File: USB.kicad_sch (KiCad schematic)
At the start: 54 parts, among them J3 USB_C_Receptacle_USB2.0, J4 USB_A_Stacked, Q4 BC817, U10 TPD4EUSB30, U4 CP2102N-Axx-xQFN24, U5 FSUSB30MUX, U6 FSUSB30MUX, U7 FE1.1, U8 TPD4EUSB30, U9 AP2191W, Y1 12MHz{slash}10pF

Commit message: Weeded out all ERC errors
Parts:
- removed C10, C9: 4u7, Capacitor_SMD:C_0402_1005Metric, symbol Device:C_Small
- removed C11, C112, C113, C12, C4: 100n, Capacitor_SMD:C_0402_1005Metric, symbol Device:C_Small
- removed C111: 10u, Capacitor_SMD:C_0805_2012Metric, symbol Device:C_Small
- removed C6: 1u, Capacitor_SMD:C_0402_1005Metric, symbol Device:C_Small
- removed D30, D31: CDBQR0130L, Diode_SMD:D_0402_1005Metric, symbol Device:D_Schottky_Small
- removed J4: USB_A_Stacked, Connector_USB:USB_A_Wuerth_61400826021_Horizontal_Stacked, symbol Yellow:USB_A_Stacked
- removed JP1: Conn_01x03_Male, Connector_PinHeader_2.54mm:PinHeader_1x03_P2.54mm_Vertical, symbol Jumper:Jumper_3_Bridged12
- removed Q4: BC817, Package_TO_SOT_SMD:SOT-23, symbol Transistor_BJT:BC817
- removed R27: 10R, Resistor_SMD:R_0402_1005Metric, symbol Device:R_Small
- removed R28, R54: 0R, Resistor_SMD:R_0402_1005Metric, symbol Device:R_Small
- removed R3, R55: 1k, Resistor_SMD:R_0402_1005Metric, symbol Device:R_Small
- removed R4, R6, R7: 2k2/1%, Resistor_SMD:R_0402_1005Metric, symbol Device:R_Small
- removed R41: 100R, Resistor_SMD:R_0402_1005Metric, symbol Device:R_Small
- removed R5: 3k6, Resistor_SMD:R_0402_1005Metric, symbol Device:R_Small
- removed R61, R8: 10k, Resistor_SMD:R_0402_1005Metric, symbol Device:R_Small
- removed TP2, TP3: TestPoint, TestPoint:TestPoint_Pad_D1.0mm, symbol Connector:TestPoint
- removed U4: CP2102N-Axx-xQFN24, Package_DFN_QFN:QFN-24-1EP_4x4mm_P0.5mm_EP2.6x2.6mm, symbol Interface_USB:CP2102N-Axx-xQFN24
- removed U5: FSUSB30MUX, Package_SO:MSOP-10_3x3mm_P0.5mm, symbol Yellow:FSUSB30MUX
- removed U7: FE1.1, Package_QFP:TQFP-48_7x7mm_P0.5mm, symbol Yellow:FE1.1
- removed U9: AP2191W, Package_TO_SOT_SMD:SOT-23-5, symbol Power_Management:AP2171W
- added C314: 100nF, Capacitor_SMD:C_0402_1005Metric, symbol Device:C_Small
- added J302, J303: USB_A, Hatlabs:USB-A-TH_ZCJB-HJ, symbol Connector:USB_A
- added Q301: BC817, Package_TO_SOT_SMD:SOT-23, symbol Transistor_BJT:BC817
- added R301: 2.7k, Resistor_SMD:R_0603_1608Metric, symbol Device:R_Small
- added R302: 1k, Resistor_SMD:R_0402_1005Metric, symbol Device:R_Small
- added R306: 10k, Resistor_SMD:R_0402_1005Metric, symbol Device:R_Small
- added R308: 15k, Resistor_SMD:R_0402_1005Metric, symbol Device:R_Small
- added U302: FE1.1S-BQFN24B, Package_DFN_QFN:QFN-24-1EP_4x4mm_P0.5mm_EP2.5x2.5mm, symbol Hatlabs:FE1.1S-BQFN24B
- added U305: AP22653W6-7, Package_TO_SOT_SMD:SOT-23-6, symbol Hatlabs:AP22653
- C301: renamed from C2; value 100n -> 100nF; LCSC (none) -> C1525
- C302: renamed from C7; value 10p -> 10pF; LCSC (none) -> C32949
- C303: renamed from C8; value 10p -> 10pF; LCSC (none) -> C32949
- C304: renamed from C1; value 100n -> 100nF; LCSC (none) -> C1525
- C305: renamed from C5; value 10u -> 10uF; LCSC (none) -> C15850
- C306: renamed from C3; value 100n -> 100nF; LCSC (none) -> C1525
- C307: renamed from C17; value 47u -> 47uF; LCSC (none) -> C16780
- C308: renamed from C18; value 47u -> 47uF; LCSC (none) -> C16780
- C309: renamed from C14; value 10u -> 10uF; LCSC (none) -> C15850
- C310: renamed from C19; value 10u -> 10uF; LCSC (none) -> C15850
- C311: renamed from C15; value 100n -> 100nF; LCSC (none) -> C1525
- C312: renamed from C20; value 10u -> 10uF; LCSC (none) -> C15850
- C313: renamed from C21; value 100n -> 100nF; LCSC (none) -> C1525
- J301: renamed from J3; footprint Connector_USB:USB_C_Receptacle_HRO_TYPE-C-31-M-12 -> HALSER:Shou Han Type-C 16P LTH6.8; symbol Connector:USB_C_Receptacle_USB2.0 -> Connector:USB_C_Receptacle_USB2.0_16P; LCSC (none) -> C5187468; Manufacturer HRO -> (none); PartNumber TYPE-C-31-M-12 -> (none)
- R303: renamed from R11; value 2.7k/1% -> 2.7k; footprint Resistor_SMD:R_0402_1005Metric -> Resistor_SMD:R_0603_1608Metric; LCSC (none) -> C13167
- R304: renamed from R13; value 5k1 -> 5.1k; LCSC (none) -> C25905
- R305: renamed from R14; value 5k1 -> 5.1k; LCSC (none) -> C25905
- R310: renamed from R62; LCSC (none) -> C25744
- U301: renamed from U6; value FSUSB30MUX -> TP3USB30M10; LCSC (none) -> C2959840; Manufacturer ON Semiconductor -> TECH PUBLIC; PartNumber FSUSB30MUX -> TP3USB30M10
- U303: renamed from U8; LCSC (none) -> C558427
- U304: renamed from U10; LCSC (none) -> C558427
- Y301: renamed from Y1; value 12MHz/10pF -> 12MHz/10pF; LCSC (none) -> C50430
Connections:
- net OTG.D+ is gone; now on net USB-C.D+: U301.3 (HSD2+)
- net OTG.D- is gone; now on net USB-C.D-: U301.7 (HSD2-)
- net +3V3: now also C304.2, C305.2, U302.16 (~{XRSTJ}), U302.17 (VBUSM), U302.18 (BUSJ), U302.20 (VD33F); no longer C304.1, C305.1
- net +5V: now also C309.1, C311.1, U305.1 (IN); no longer C309.2, C311.2
- net GND: now also C304.1, C305.1, C309.2, C311.2, C314.2, J302.4 (GND), J302.5 (Shield), J303.4 (GND), J303.5 (Shield), Q301.2 (E), R301.1, R308.2, U302.25 (VSS), U305.2 (GND); no longer C304.2, C305.2, C309.1, C311.1
- net HUB.D+: now also U302.15 (DPU)
- net HUB.D-: now also U302.14 (DMU)
- net USB0.D+: now also J302.3 (D+), U302.10 (DP2)
- net USB0.D-: now also J302.2 (D-), U302.9 (DM2)
- net USB1.D+: now also J303.3 (D+), U302.12 (DP1)
- net USB1.D-: now also J303.2 (D-), U302.11 (DM1)
- net VBUS: now also R301.2
- net VBUS_{OUT}: now also C314.1, J302.1 (VBUS), J303.1 (VBUS), U305.6 (OUT)
- net ~{USB_OC}: now also U302.1 (~{OVCJ}), U305. (~{FAULT})
- net at C302.1, Y301.3: now also U302.3 (XOUT)
- net at C303.1, Y301.1: now also U302.4 (XIN)
- net at R303.2: now also U302.13 (REXT)
- net CM4_USB_D+ renamed D+
- net CM4_USB_D- renamed D-
- net CM4_USB_OTG_ID renamed OTG_ID
- new net: Q301.1 (B), R302.1
- new net: R308.1, U305.5 (ILIM)
- new net CMx_3V3: R306.1
- new net EN: Q301.3 (C), R306.2, U305.3 (EN)
- new net ~{USB_PWR_EN}: R302.2, U302.24 (~{PWRJ})
- no-connect marks 26 -> 12
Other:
- note added: "AP22653 EN is active-high."
- note added: "USB-C Receptacle and ESD protection USB 2.0 Peripheral operation only"
- note removed: "CP2102N USB <-> UART For CM4 serial console"
- note removed: "For break signalling"
- note removed: "NOTE: Place 10uF cap. close to the pin 26 and 0.1uF close to pin 3, 13."
- note removed: "USB-C Receptacle and ESD protection USB 2.0 Peripheral operataion only"
- note removed: "USB-C peripheral mode selection switch 1-2 USB-C <-> CP2102N 3-2 USB-C <-> CM4 OTG"
- company: Nabu Casa -> Hat Labs Oy
- title: USB 2.0 host/USB 2.0 device -> HALPI2
- moved on the sheet: C301, C302, C303, C304, C305, C306, C307, C308, C309, C310, C311, C312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

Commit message: Implement ideal diodes for input and LDO power ORing
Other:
- note added: "MUX selecting between USB peripheral and host mode (using different ports as well)"
- note added: "USB 2.0 HUB for host mode use"
- moved on the sheet: C301, C302, C303, C304, C305, C306, C309, C311, J301, R301, R303, R304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

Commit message: Re-annotate schematics
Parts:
- renumbered C306 to C305, C305 to C306, C309 to C307, C307 to C309, C311 to C310, C312 to C311, C310 to C312, C314 to C313, C313 to C314, R303 to R302, R304 to R303, R305 to R304, R302 to R305, R308 to R307, R310 to R308

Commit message: Sprinkle test points on the schematics
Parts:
- added TP301, TP302, TP303: TestPoint, TestPoint:TestPoint_Pad_D1.0mm, symbol Connector:TestPoint
- J301: footprint HALSER:Shou Han Type-C 16P LTH6.8 -> Hatlabs:USB_TYPE-C_SHOU-HAN_16PLT-H6.8
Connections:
- net VBUS_{OUT}: now also TP303.1
- net ~{USB_OC}: now also TP302.1
- net ~{USB_PWR_EN}: now also TP301.1

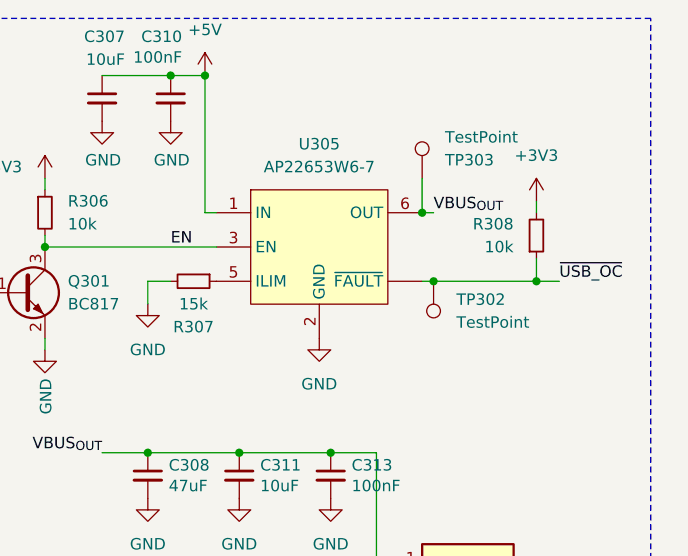
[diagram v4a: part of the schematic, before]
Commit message: Fix ethernet port & other changes
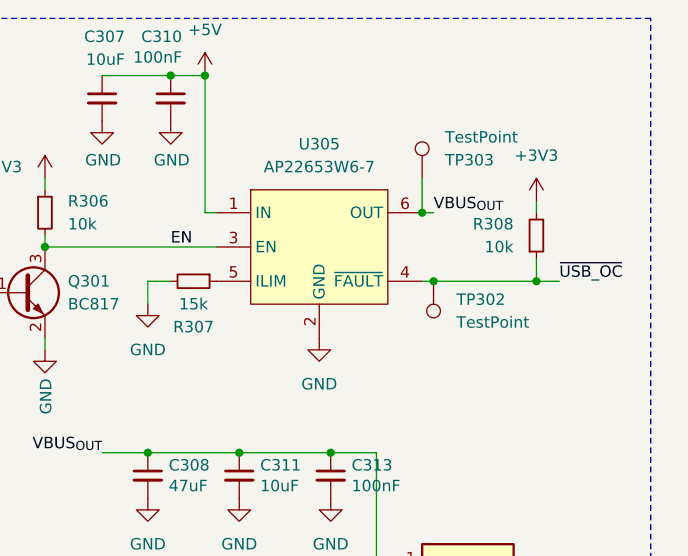
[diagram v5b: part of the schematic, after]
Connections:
- net ~{USB_OC}: now also U305.4 (~{FAULT}); no longer U305. (~{FAULT})
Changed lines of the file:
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@@
 			)
 		)
-		(pin ""
+		(pin "4"
 		)
 		(pin "5"

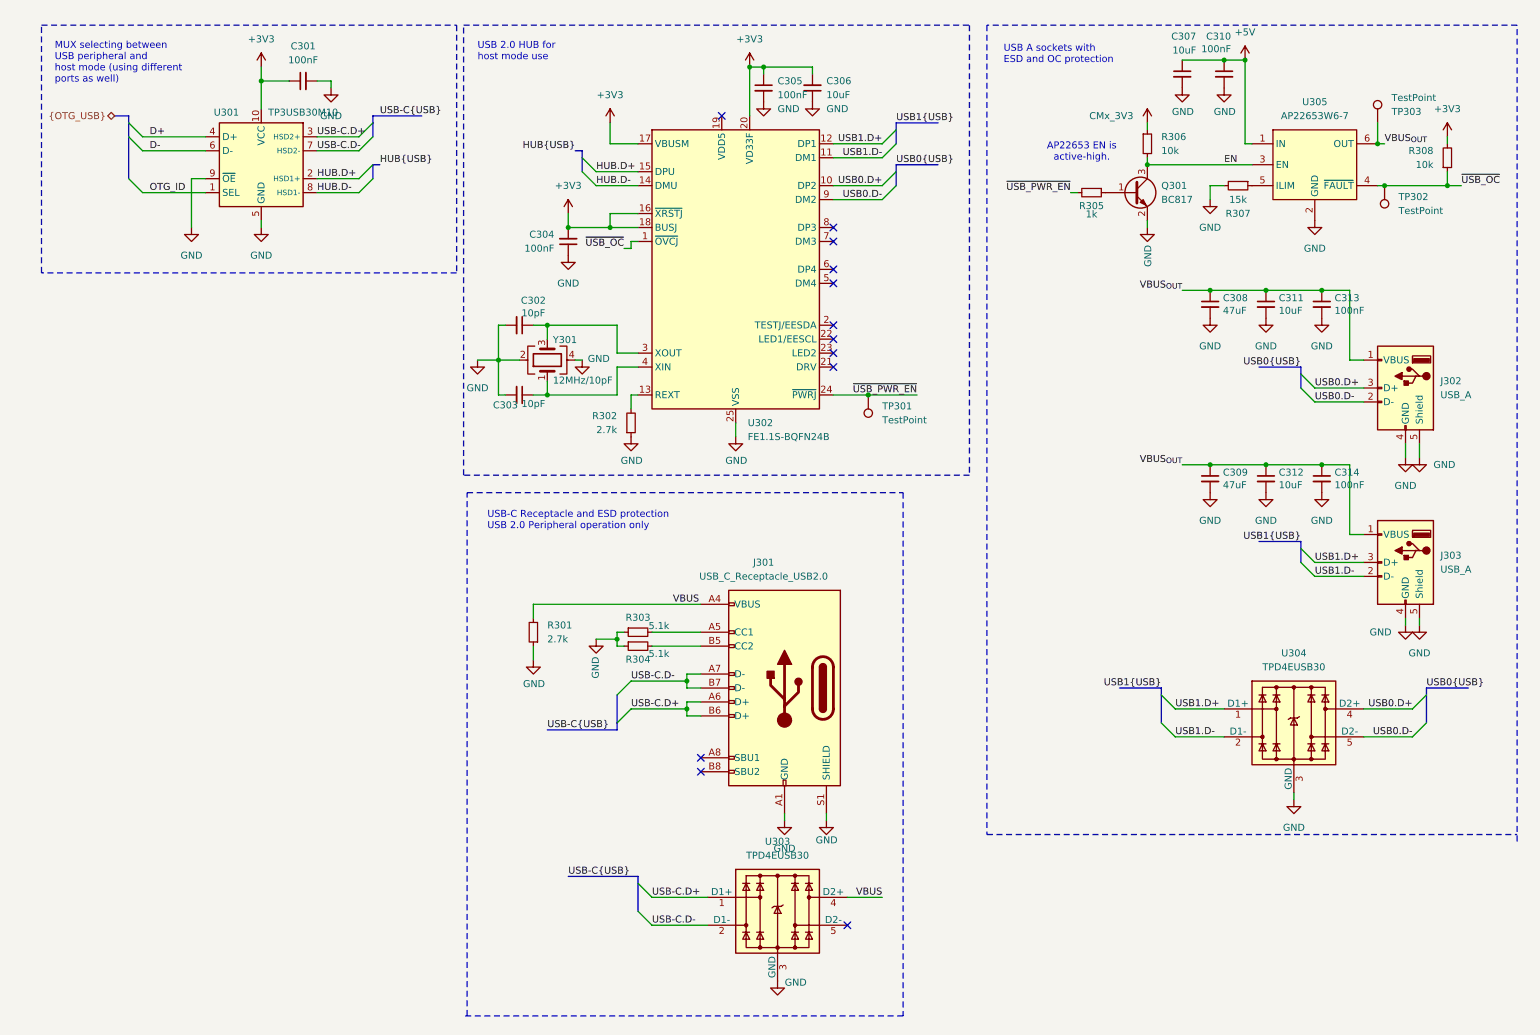
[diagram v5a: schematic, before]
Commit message: Reserve USB 2 for peripheral use only
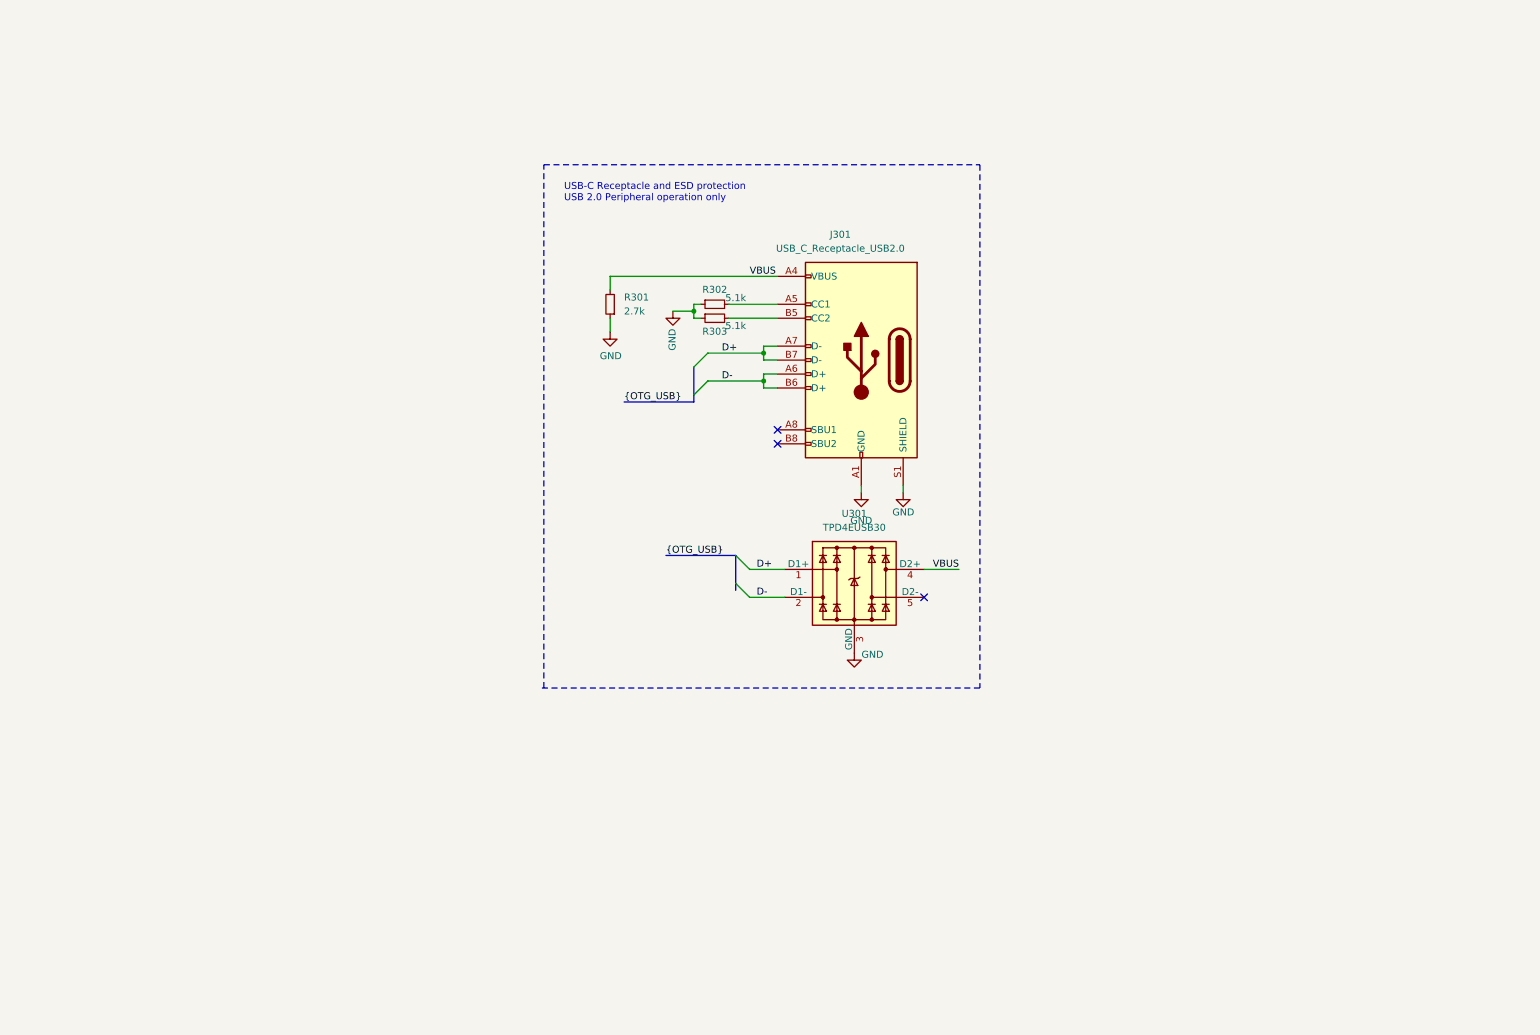
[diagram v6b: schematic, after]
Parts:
- removed C301, C304, C305, C310, C313, C314: 100nF, Capacitor_SMD:C_0402_1005Metric, symbol Device:C_Small
- removed C302, C303: 10pF, Capacitor_SMD:C_0402_1005Metric, symbol Device:C_Small
- removed C306, C307, C311, C312: 10uF, Capacitor_SMD:C_0805_2012Metric, symbol Device:C_Small
- removed C308, C309: 47uF, Capacitor_SMD:C_0805_2012Metric, symbol Device:C_Small
- removed J302, J303: USB_A, Hatlabs:USB-A-TH_ZCJB-HJ, symbol Connector:USB_A
- removed Q301: BC817, Package_TO_SOT_SMD:SOT-23, symbol Transistor_BJT:BC817
- removed R304: 5.1k, Resistor_SMD:R_0402_1005Metric, symbol Device:R_Small
- removed R305: 1k, Resistor_SMD:R_0402_1005Metric, symbol Device:R_Small
- removed R306, R308: 10k, Resistor_SMD:R_0402_1005Metric, symbol Device:R_Small
- removed R307: 15k, Resistor_SMD:R_0402_1005Metric, symbol Device:R_Small
- removed TP301, TP302, TP303: TestPoint, TestPoint:TestPoint_Pad_D1.0mm, symbol Connector:TestPoint
- removed U301: TP3USB30M10, Package_SO:MSOP-10_3x3mm_P0.5mm, symbol Yellow:FSUSB30MUX
- removed U302: FE1.1S-BQFN24B, Package_DFN_QFN:QFN-24-1EP_4x4mm_P0.5mm_EP2.5x2.5mm, symbol Hatlabs:FE1.1S-BQFN24B
- removed U303, U304: TPD4EUSB30, Package_SON:USON-10_2.5x1.0mm_P0.5mm, symbol Yellow:TPD4EUSB30
- removed U305: AP22653W6-7, Package_TO_SOT_SMD:SOT-23-6, symbol Hatlabs:AP22653
- removed Y301: 12MHz/10pF, Crystal:Crystal_SMD_3225-4Pin_3.2x2.5mm, symbol Device:Crystal_GND24
- added U301: TPD4EUSB30, Package_SON:USON-10_2.5x1.0mm_P0.5mm, symbol Yellow:TPD4EUSB30
- R302: value 2.7k -> 5.1k; footprint Resistor_SMD:R_0603_1608Metric -> Resistor_SMD:R_0402_1005Metric; LCSC C13167 -> C25905
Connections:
- net USB-C.D+ is gone; now on net D-: J301.A6 (D+), J301.B6 (D+)
- net USB-C.D- is gone; now on net D+: J301.A7 (D-), J301.B7 (D-)
- net D+: now also U301.1 (D1+), U301.10 (D1+)
- net D-: now also U301.2 (D1-), U301.9 (D1-)
- net GND: now also U301.3 (GND), U301.8 (GND)
- net VBUS: now also U301.4 (D2+), U301.7 (D2+)
- net at J301.B5 (CC2): now also R303.2
- net at R302.2: now also J301.A5 (CC1)
- new net: U301.5 (D2-), U301.6 (D2-)
- no-connect marks 12 -> 3
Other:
- note removed: "AP22653 EN is active-high."
- note removed: "MUX selecting between USB peripheral and host mode (using different ports as well)"
- note removed: "USB 2.0 HUB for host mode use"
- note removed: "USB A sockets with ESD and OC protection"
